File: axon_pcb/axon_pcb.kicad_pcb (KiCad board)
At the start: 2 copper layers, 227.6 x 99.2 mm, 120 parts, among them J1 USB_C_Receptacle, J2 AVR_ISP Header, K1 KEYSW, K10 KEYSW, K11 KEYSW, K12 KEYSW, K13 KEYSW, K14 KEYSW, K15 KEYSW, K16 KEYSW, K17 KEYSW, K18 KEYSW, K19 KEYSW, K2 KEYSW, K20 KEYSW, K21 KEYSW, K22 KEYSW, K23 KEYSW, K24 KEYSW, K25 KEYSW, K26 KEYSW, K27 KEYSW, K28 KEYSW, K29 KEYSW, K3 KEYSW, K30 KEYSW, K31 KEYSW, K32 KEYSW, K33 KEYSW, K34 KEYSW, K35 KEYSW, K36 KEYSW, K37 KEYSW, K38 KEYSW, K39 KEYSW, K4 KEYSW, K40 KEYSW, K5 KEYSW, K6 KEYSW, K7 KEYSW, K8 KEYSW, K9 KEYSW, SW1 RESET, SW2 BOOT, U1 ATmega328P-PU, X1 16MHz

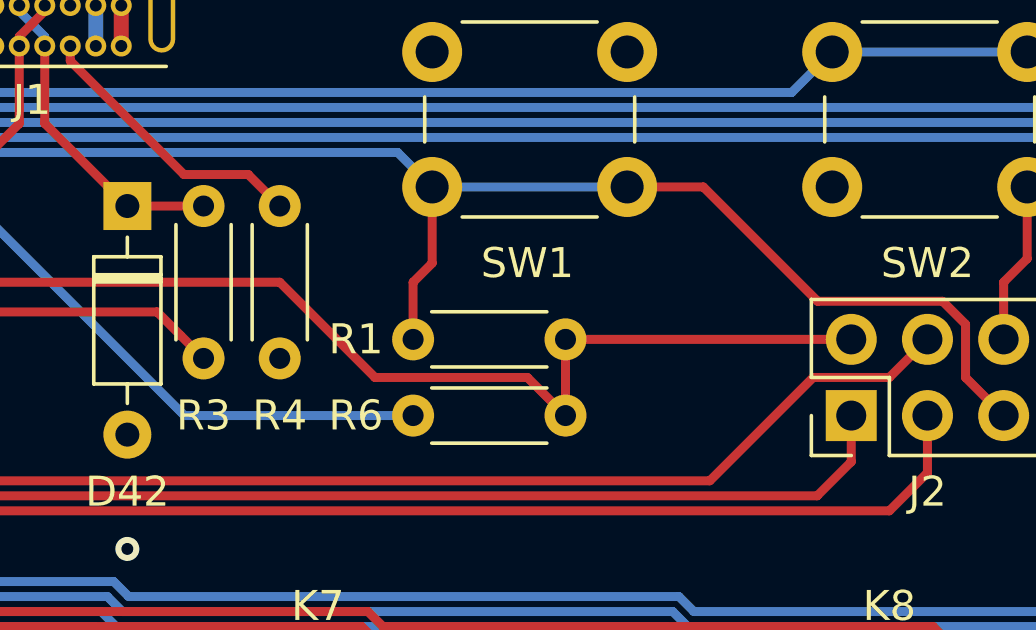
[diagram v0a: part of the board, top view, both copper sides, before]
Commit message: added libraries used, updated readme to give credit
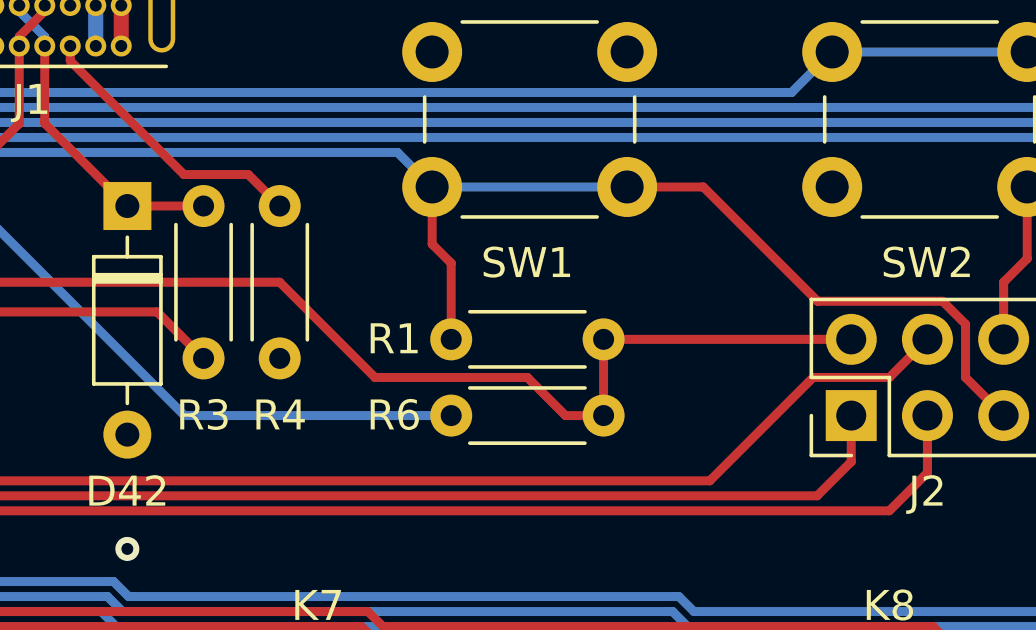
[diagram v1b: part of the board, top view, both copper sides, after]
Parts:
- moved R1 1.27 mm to (118.7, -17.1)
- moved R6 1.27 mm to (123.8, -14.6)
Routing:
- net Net-(D41-Pad1): track 29.5 -> 30.8 mm

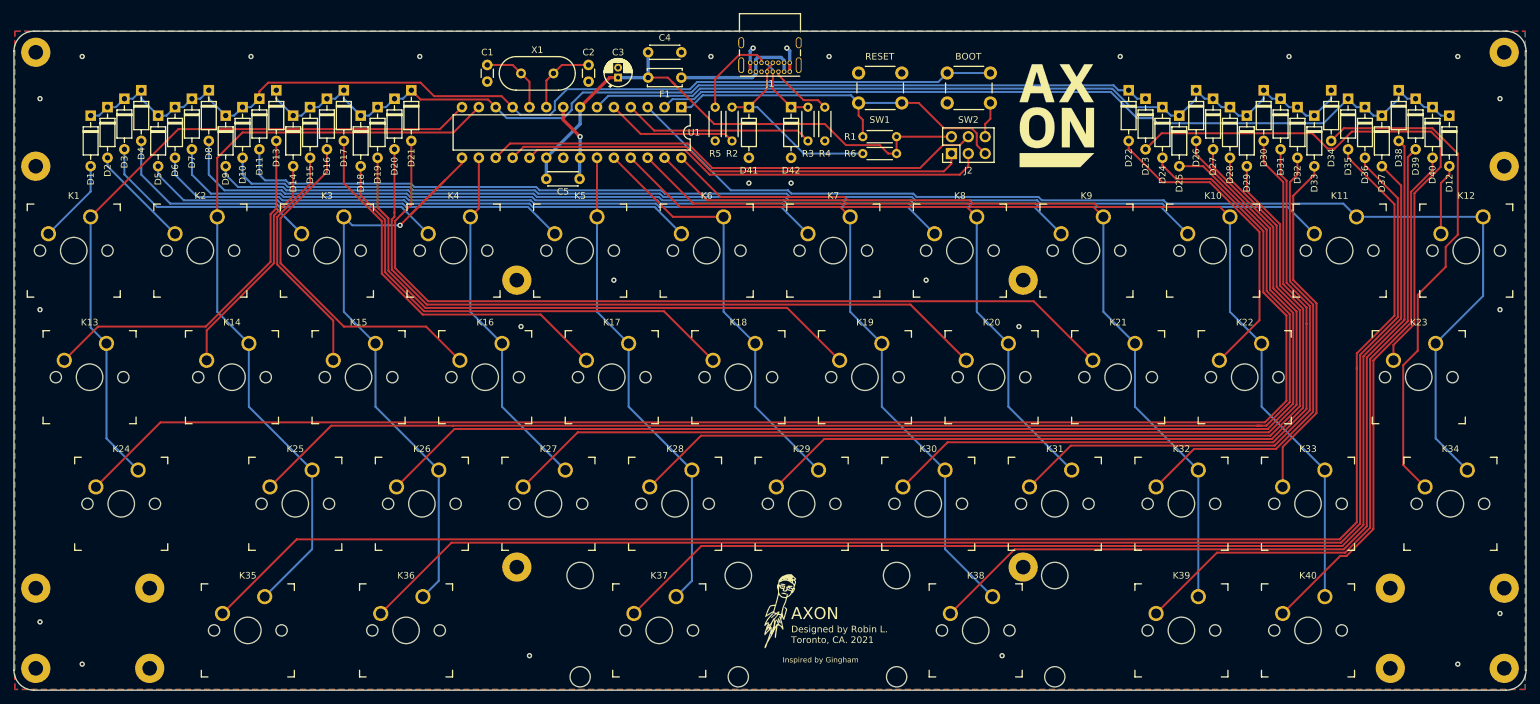
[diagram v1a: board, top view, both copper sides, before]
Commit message: tweaked component placements: - components further from edges - less difference in USB data line lengths (now less than 2 mm) - made crystal cap trace lengths more samey
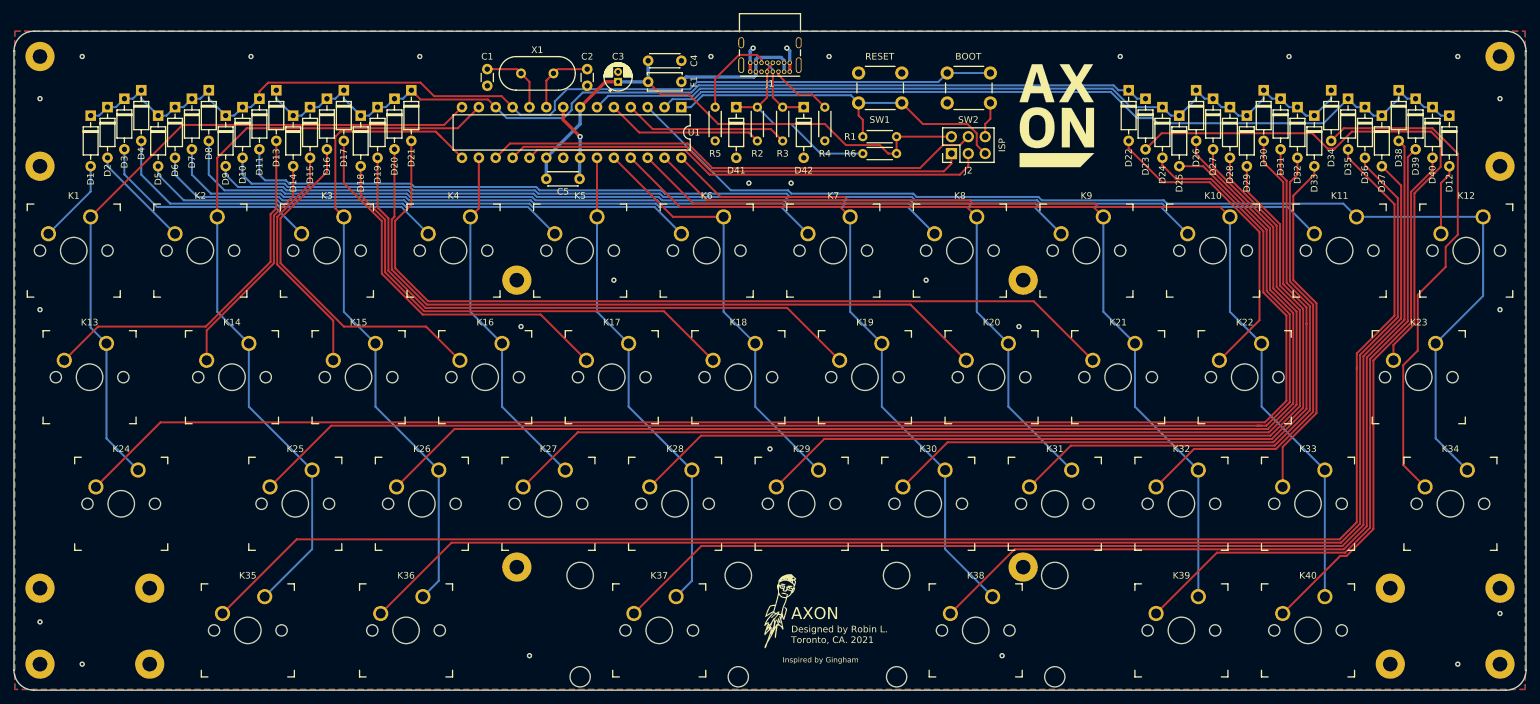
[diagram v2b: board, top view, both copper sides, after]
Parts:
- J2: footprint Connector_PinHeader_2.54mm:PinHeader_2x03_P2.54mm_Vertical -> personal:PinHeader_2x03_P2.54mm_Vertical
- moved R2 3.81 mm to (102.9, -16.5)
- moved R3 3.81 mm to (106.7, -16.5)
- moved D41 1.91 mm to (99.7, -21.6)
- moved D42 1.91 mm to (109.9, -21.6)
- moved C4 1.27 mm to (86.4, -28.6)
- moved REF** 0.90 mm to (-5.08, 62.2)
- moved REF** 0.90 mm to (-5.08, -29.2)
- moved REF** 0.90 mm to (214.6, 62.2)
- moved REF** 0.90 mm to (214.6, -29.2)
- moved C2 0.67 mm to (77.3, -27.3)
- moved REF** 0.64 mm to (198.1, 62.2)
- moved REF** 0.64 mm to (11.4, 62.2)
- moved C1 0.64 mm to (62.2, -27.3)
- moved C3 0.64 mm to (81.9, -25.4)
- moved F1 0.64 mm to (91.4, -25.4)
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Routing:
- net /col2: track 94.5 -> 98.5 mm, vias 1 -> 0
- net /USB_D-: track 19.9 -> 23.7 mm
- net /USB_D+: track 28.8 -> 25.0 mm
- net +5V: track 82.2 -> 80.5 mm
- net Net-(D41-Pad1): track 30.8 -> 29.6 mm
- net GND: vias 27 -> 28
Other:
- board text added: "ALT"
- board text added: "SYS"
- board text added: "TAB / CTRL"
- board text removed: "MOD1"
- board text removed: "MOD2"
- board text removed: "MOD3"
- board text removed: "MOD4"
- board text removed: "TAB"

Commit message: fixed libraries, final pcb version
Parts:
- removed the REF** at (214.6, 50.8)
- removed the REF** at (198.1, 50.8)
- removed the REF** at (198.1, 62.2)
- removed the REF** at (-5.08, 50.8)
- removed the REF** at (11.4, 50.8)
- removed the REF** at (11.4, 62.2)
- added G***: LOGO, personal:axon_axonangular_unfilled, F.Cu at (182.9, -29.2)
- added G***: LOGO, personal:axon_axonangular_unfilled, F.Cu at (26.7, -29.2)
- moved G*** 0.49 mm to (148.4, -20.6)
- moved C5 0.25 mm to (71.1, -11.0)
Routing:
- net GND: track 24.8 -> 19.1 mm, vias 28 -> 30
- net /SCK: track 70.5 -> 69.2 mm
- net /MISO: track 70.3 -> 69.2 mm
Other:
- board text added: "BACKSPACE"
- board text added: "FUNCTION"
- board text added: "TAB"
- board text removed: "DEL"
- board text removed: "FN"
- board text removed: "TAB / CTRL"

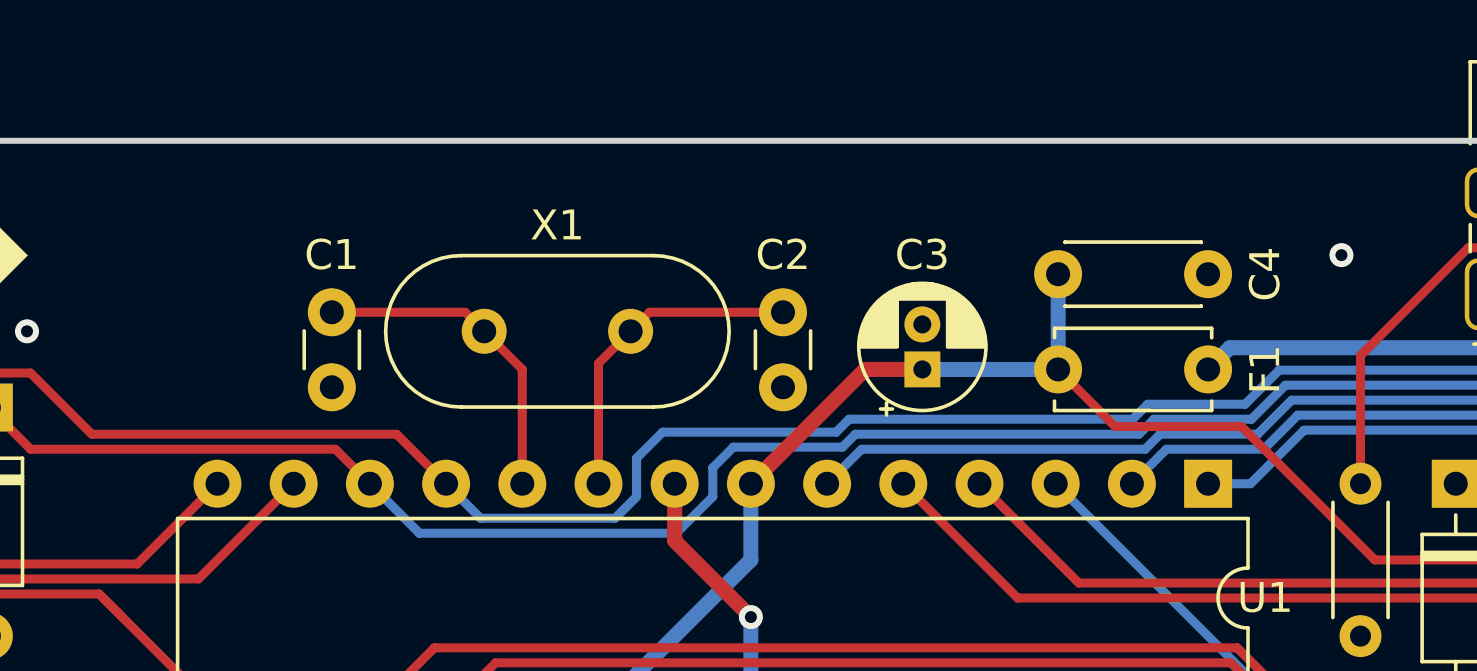
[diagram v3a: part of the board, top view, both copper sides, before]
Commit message: updated capacitor placement
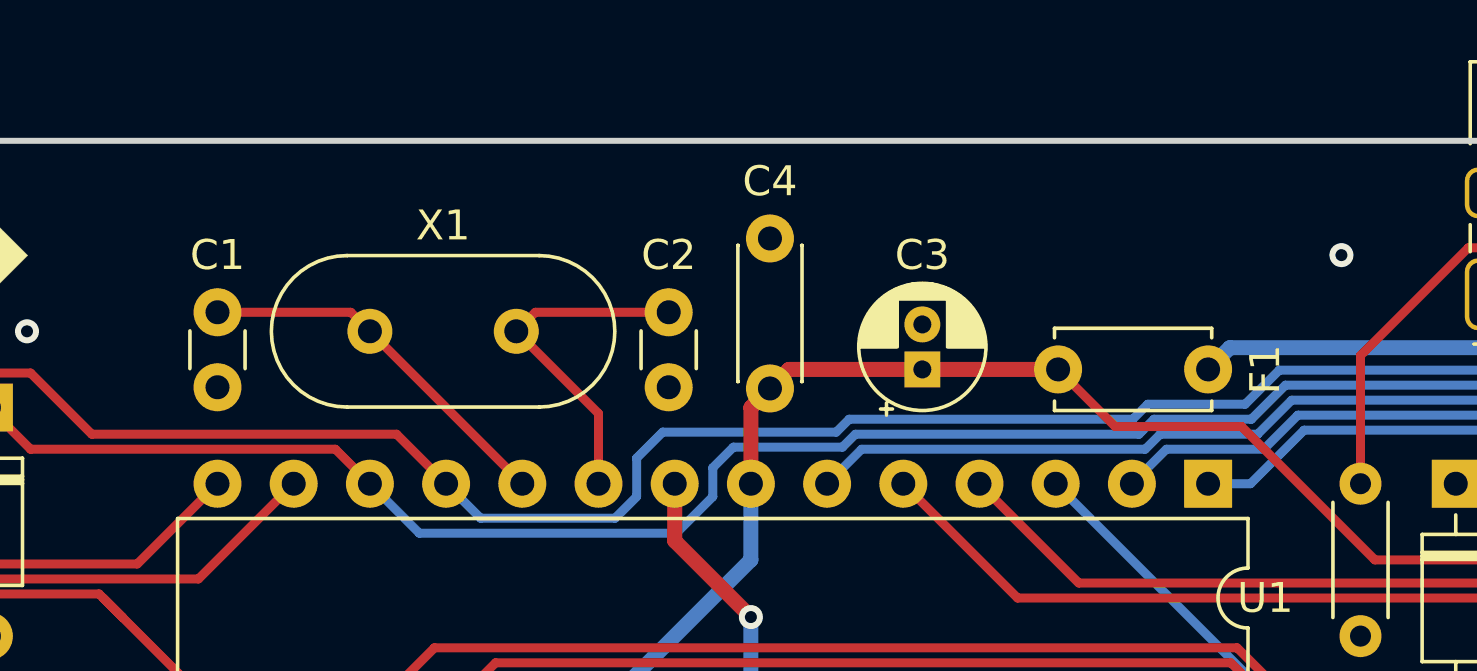
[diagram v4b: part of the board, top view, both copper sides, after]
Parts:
- moved C4 10.3 mm to (76.8, -24.8), turned to 90 degrees
- moved C2 3.81 mm to (73.5, -27.3)
- moved X1 3.81 mm to (63.5, -26.7)
- moved C1 3.81 mm to (58.4, -27.3)
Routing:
- net +5V: track 80.3 -> 78.6 mm
- net Net-(C1-Pad1): track 10.9 -> 12.5 mm
- net Net-(C2-Pad1): track 10.9 -> 11.6 mm

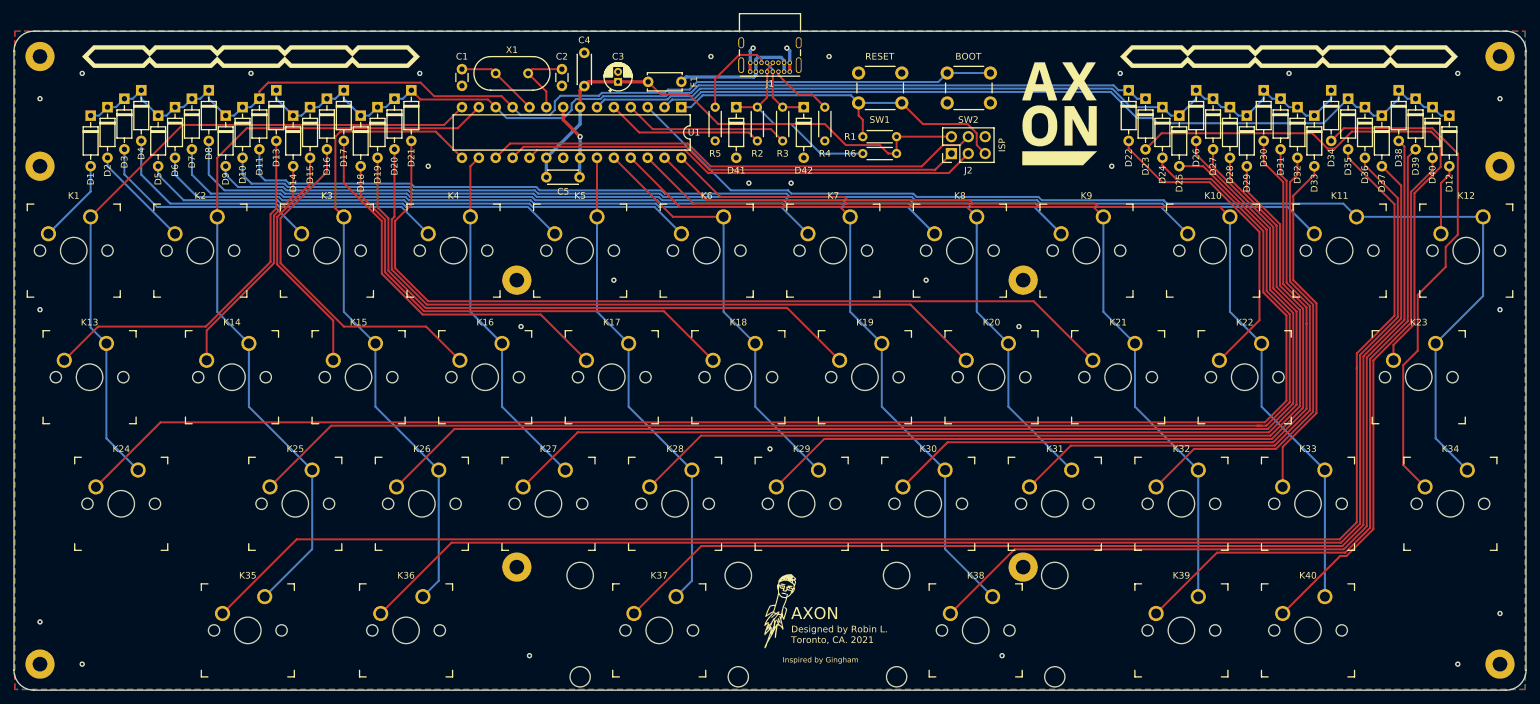
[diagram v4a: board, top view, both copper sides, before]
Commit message: rerouting and added alt spacebar config
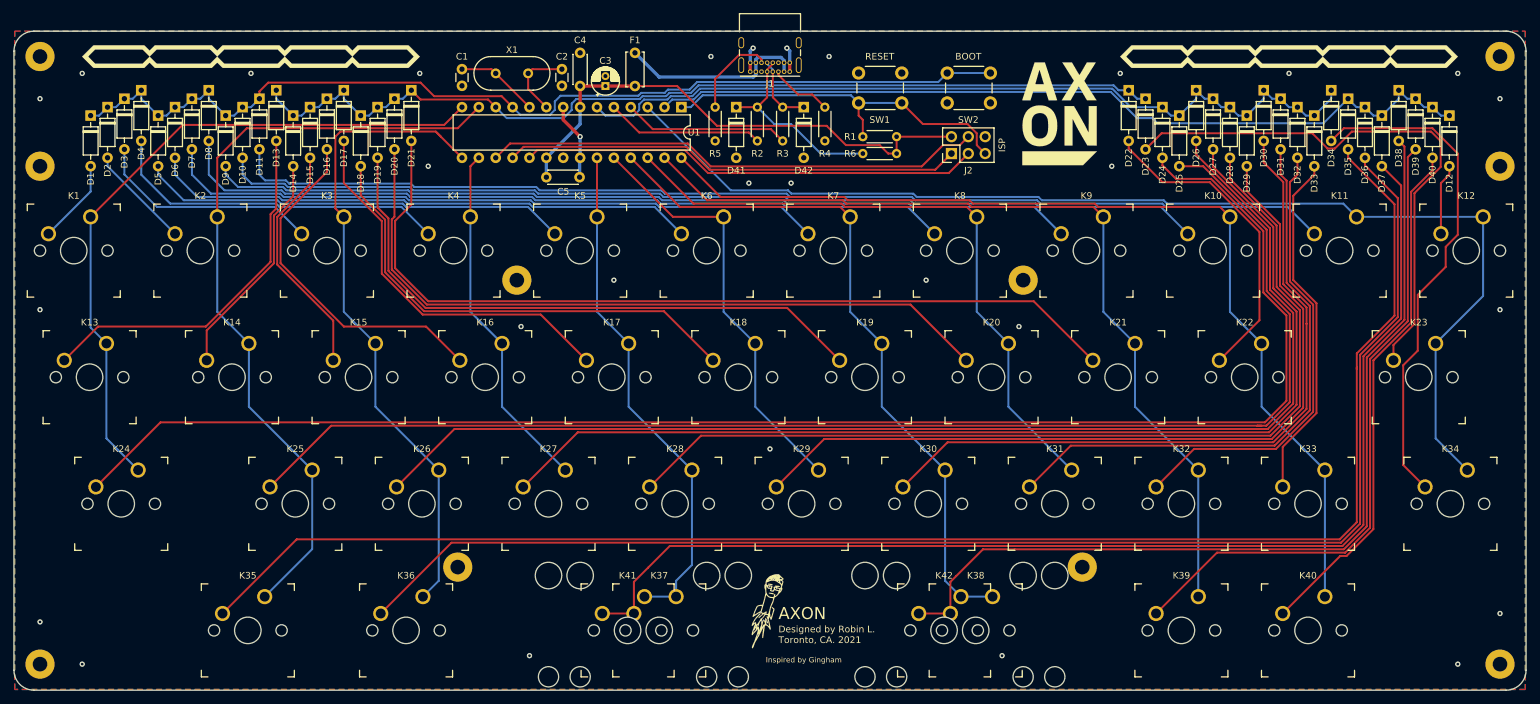
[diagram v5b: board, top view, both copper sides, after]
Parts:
- added K41: KEYSW, keyswitches-daprice:SW_MX, F.Cu at (83.3, 57.1)
- added K42: KEYSW, keyswitches-daprice:SW_MX, F.Cu at (131.0, 57.1)
- added REF**: Stabilizer_MX_2u, keyswitches-daprice:Stabilizer_MX_2u, F.Cu at (131.0, 57.1)
- added REF**: Stabilizer_MX_2u, keyswitches-daprice:Stabilizer_MX_2u, F.Cu at (83.3, 57.1)
- moved REF** 8.89 mm to (57.8, 47.6)
- moved REF** 8.89 mm to (151.8, 47.6)
- moved F1 8.24 mm to (84.5, -29.8), turned to 270 degrees
- moved C3 2.01 mm to (80.0, -24.8)
- moved G*** 1.91 mm to (104.8, 54.0)
- moved C4 0.63 mm to (76.2, -24.8)
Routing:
- net Net-(D37-Pad2): track 172.8 -> 182.0 mm
- net Net-(F1-Pad1): track 20.2 -> 28.4 mm
- net Net-(D38-Pad2): track 128.8 -> 136.4 mm
- net /col4: track 72.9 -> 77.7 mm
- net /col6: track 102.7 -> 105.5 mm
- net /row2: track 123.4 -> 125.0 mm

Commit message: board updates to fix 1.0 issues
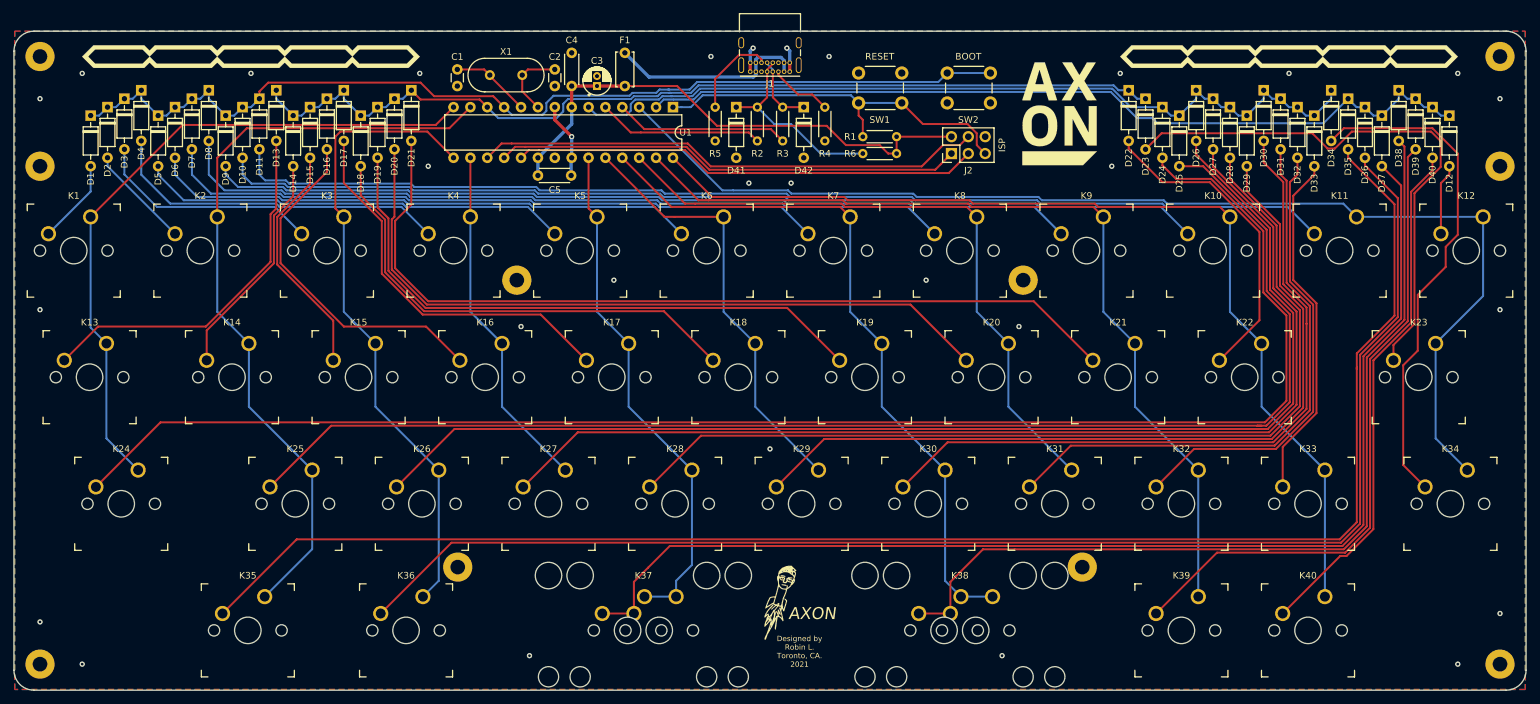
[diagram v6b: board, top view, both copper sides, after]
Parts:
- moved G*** 2.29 mm to (106.7, 52.7)
- moved F1 1.52 mm to (82.9, -29.8)
- moved C5 1.30 mm to (69.8, -11.3)
- moved C3 1.27 mm to (78.7, -24.8)
- moved C4 1.27 mm to (74.9, -24.8)
- moved U1 1.27 mm to (90.2, -21.6)
- moved C2 1.07 mm to (72.4, -27.3)
- moved X1 0.92 mm to (62.6, -26.4)
- moved C1 0.70 mm to (57.7, -27.3)
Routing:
- net /col2: track 98.5 -> 96.4 mm
- net Net-(F1-Pad1): track 28.4 -> 29.9 mm
- net /row2: track 125.0 -> 126.5 mm
- net /row3: track 127.5 -> 128.8 mm
- net /col8: track 132.8 -> 134.1 mm
- net /col1: track 117.4 -> 116.2 mm
- net /col0: track 103.8 -> 102.5 mm
- net /SCK: track 69.2 -> 70.4 mm
- net /USB_D-: track 23.7 -> 25.0 mm
- net /col6: track 105.5 -> 106.8 mm
- net /col5: track 64.2 -> 65.5 mm
- net /USB_D+: track 25.0 -> 26.2 mm
- net /RESET: track 56.5 -> 57.7 mm
- net /MOSI: track 75.3 -> 76.6 mm
- net /MISO: track 69.2 -> 70.4 mm
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
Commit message: update readme, change rear silk to reflect default keymap
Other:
- board text added: "CTRL"
- board text removed: "SYS"
